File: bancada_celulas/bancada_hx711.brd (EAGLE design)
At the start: 124.5 x 102.9 mm, 21 parts, among them J1 J5MM, J2 J5MM, J3 J5MM, J4 J5MM, X1 22-23-2041, X10 22-23-2021, X11 22-23-2041, X2 22-23-2041, X3 22-23-2041, X4 22-23-2041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

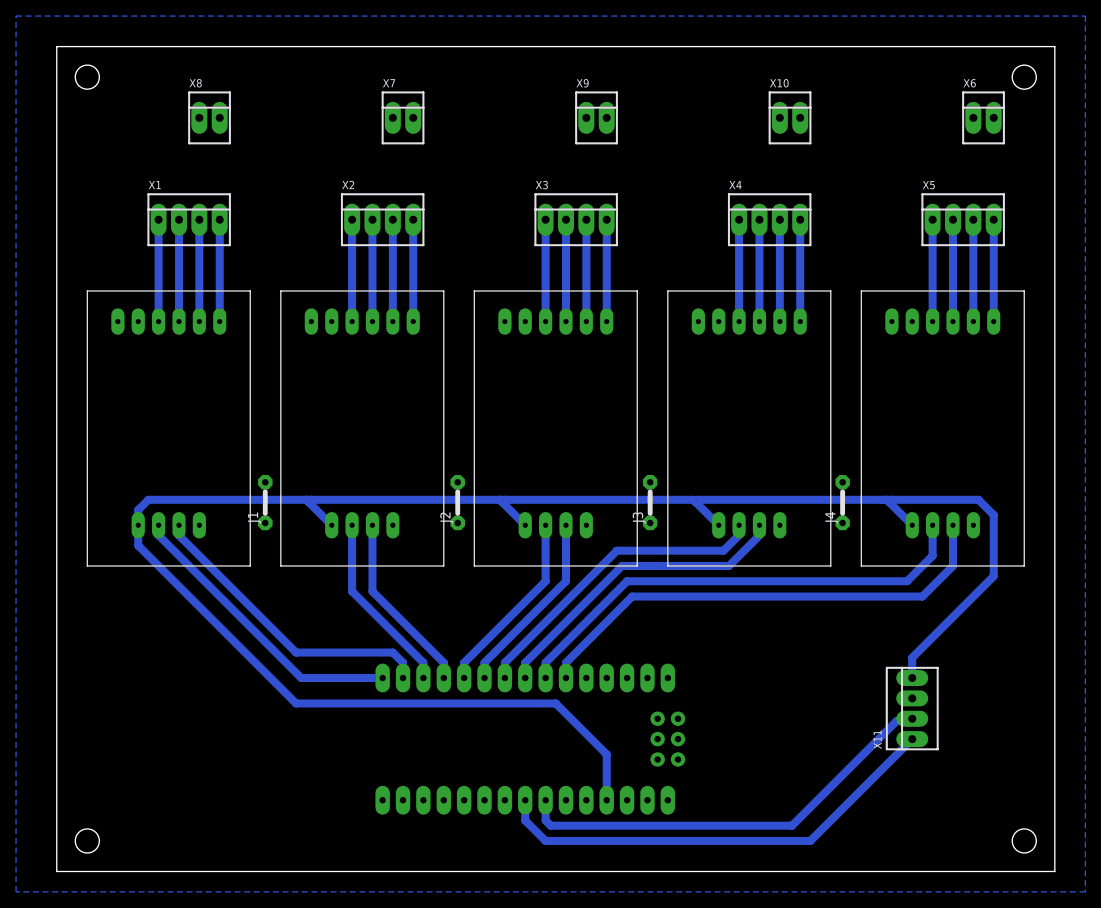
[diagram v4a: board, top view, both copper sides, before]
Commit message: Change board edges and holes
Edges and holes are supossed to be in "mm", different from the components and traces, that should follow "mil" units. 

This way we the board respects the board manufacturer (who uses mil system) as well as the CAD designer (who uses metric system).
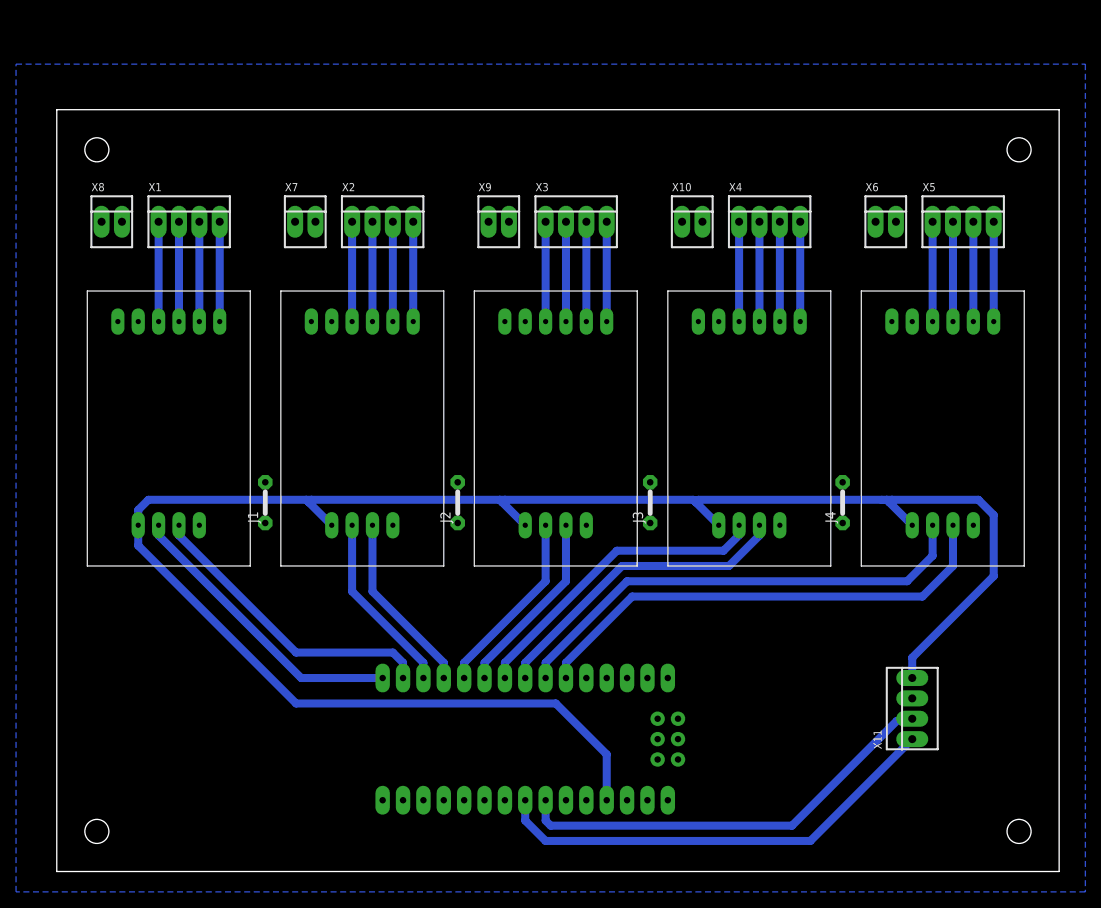
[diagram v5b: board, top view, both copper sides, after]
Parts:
- moved X7 17.8 mm to (31.0, 81.0)
- moved X8 17.8 mm to (6.86, 81.0)
- moved X9 17.8 mm to (55.1, 81.0)
- moved X10 17.8 mm to (79.2, 81.0)
- moved X6 17.8 mm to (103.4, 81.0)
- moved X1 0.25 mm to (16.5, 81.0)
- moved X2 0.25 mm to (40.6, 81.0)
- moved X3 0.25 mm to (64.8, 81.0)
- moved X4 0.25 mm to (88.9, 81.0)
- moved X5 0.25 mm to (113.0, 81.0)
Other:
- board size 124.5 x 102.9 mm -> 125 x 95 mm
